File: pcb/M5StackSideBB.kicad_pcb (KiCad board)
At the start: 2 copper layers, 100 x 50 mm, 16 parts, among them J1 Conn_01x11, J2 Conn_01x11, J3 Conn_02x15_Odd_Even, J4 Conn_02x15_Odd_Even

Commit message: Change back logo size larger
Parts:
- removed G1: LOGO, logo:halake_25p5x18@5mm
- added G***: LOGO, logo:halake_44x32mm, B.Cu at (175.8, 77.4)

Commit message: Update design for production
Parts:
- removed G***: LOGO, logo:halake_44x32mm
- removed G2: LOGO, logo:halake_8p7px6p3mm
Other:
- board text added: "Rev 2018.08"
- board text added: "https://github.com/asukiaaa/M5StackSideBB"
- board text removed: "Rev 1.2"

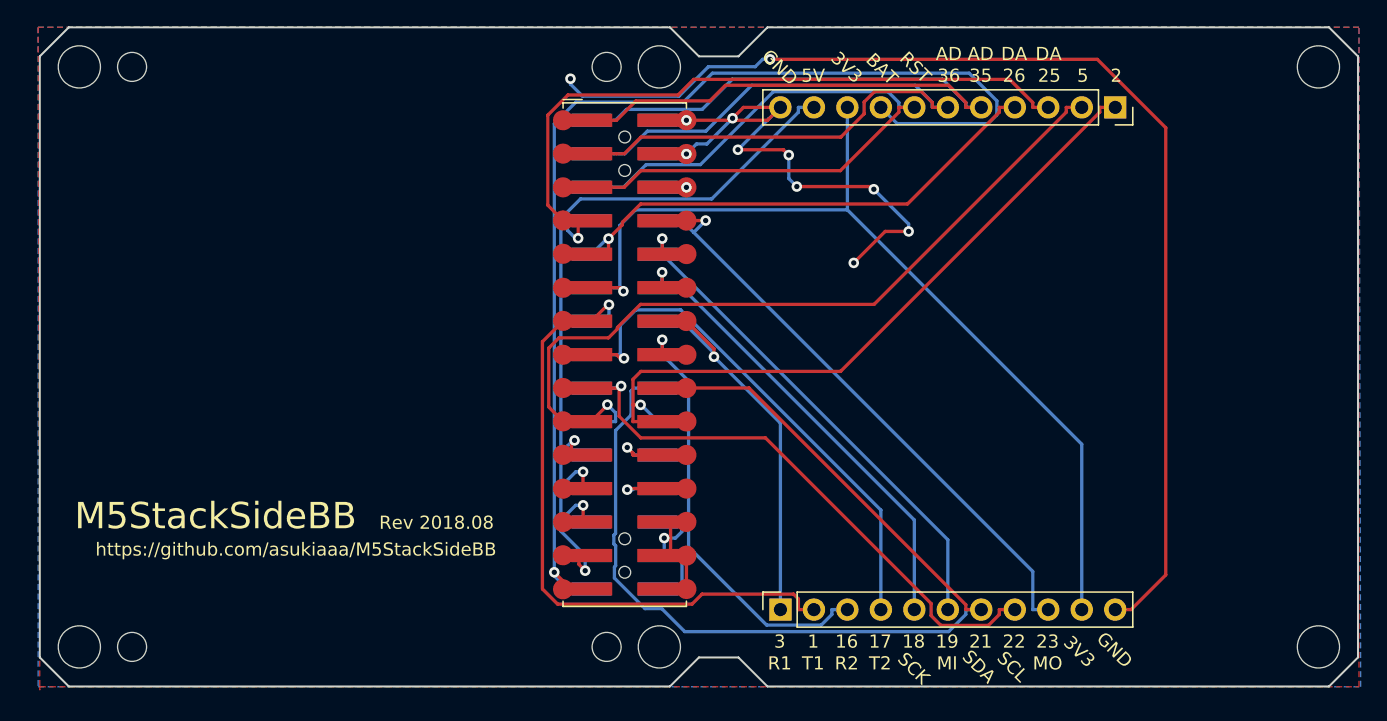
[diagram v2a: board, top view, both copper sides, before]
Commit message: Change pad position as Rev 2018.11
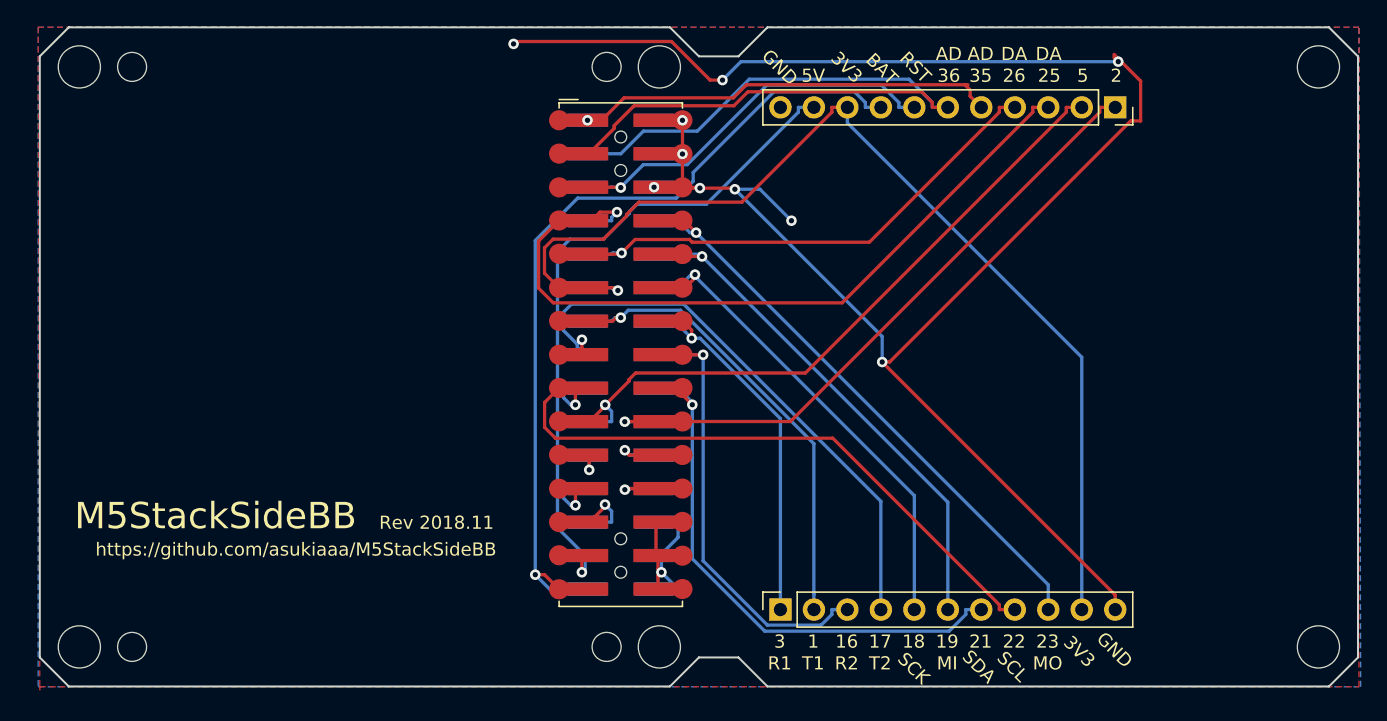
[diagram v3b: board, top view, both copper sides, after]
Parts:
- moved J3 0.30 mm to (144.1, 74.8)
- moved J4 0.30 mm to (144.1, 74.8)
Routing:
- net G21: track 79.1 -> 44.1 mm, vias 0 -> 1
- net G35: track 65.7 -> 34.4 mm, vias 0 -> 1
- net RST: track 57.6 -> 33.6 mm, vias 0 -> 1
- net +BATT: track 87.9 -> 66.5 mm
- net G1: track 49.7 -> 39.1 mm
- net +3V3: track 75.2 -> 83.6 mm
- net G5: track 61.6 -> 53.3 mm
- net GND: track 145.6 -> 153.5 mm, vias 12 -> 10
- net G22: track 46.8 -> 52.5 mm
- net G2: track 55.0 -> 49.5 mm
- net G17: track 43.6 -> 46.8 mm
- net G25: track 55.8 -> 58.6 mm
- net G13: track 6.60 -> 4.77 mm
- net G23: track 48.4 -> 46.8 mm
- net G18: track 38.0 -> 39.5 mm
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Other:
- board text added: "Rev 2018.11"
- board text removed: "Rev 2018.08"

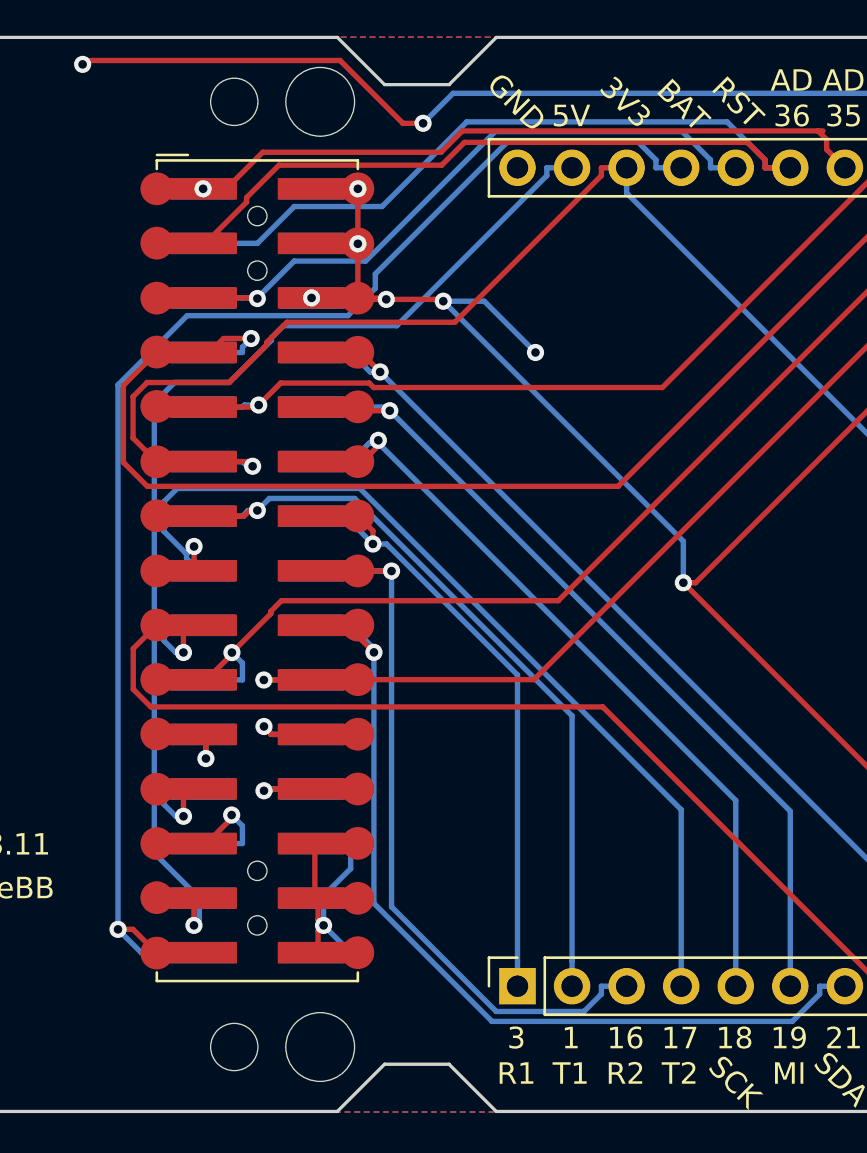
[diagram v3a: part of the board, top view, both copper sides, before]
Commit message: Add 4 holes to detect position of spacer_pcb
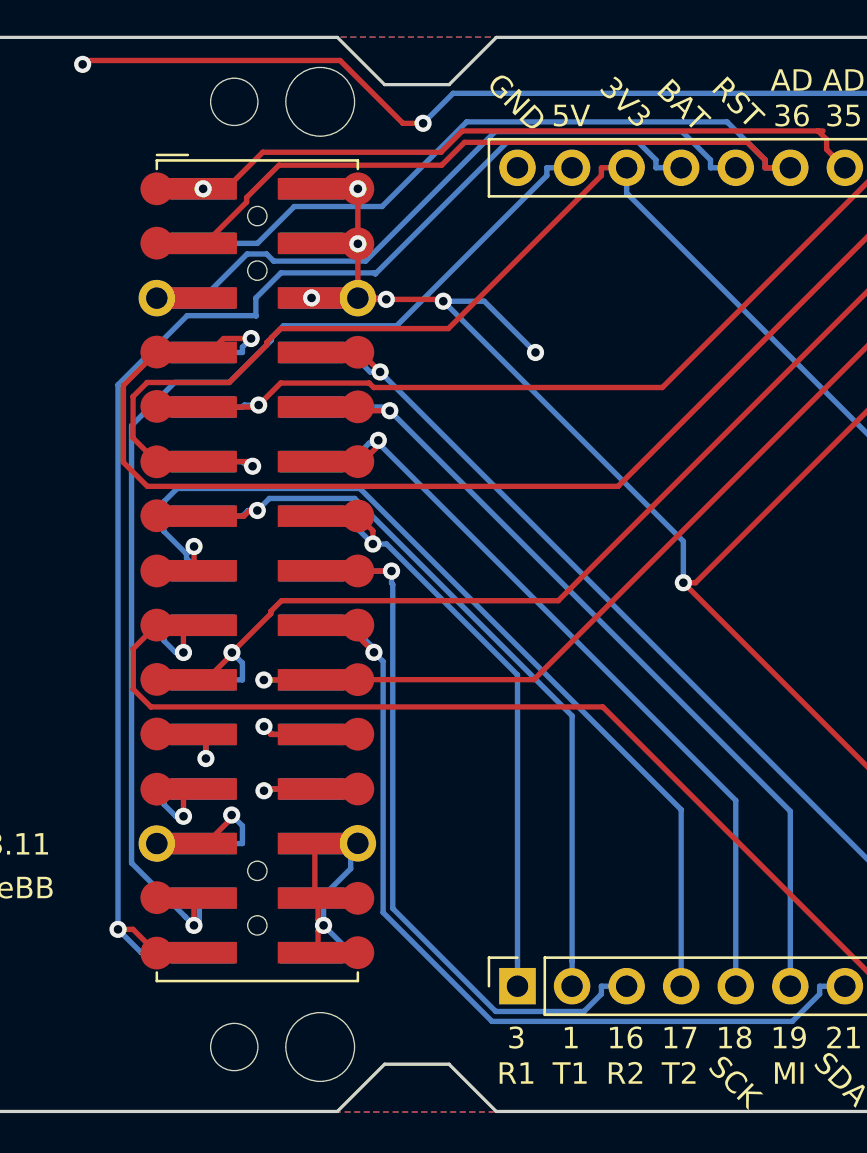
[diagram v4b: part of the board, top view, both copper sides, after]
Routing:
- net +5V: track 53.8 -> 55.8 mm
- net RST: track 33.6 -> 33.5 mm, vias 1 -> 0

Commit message: Add open source hardware logo
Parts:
- added REF**: OSHW-Logo2_7.3x6mm_SilkScreen, Symbol:OSHW-Logo2_7.3x6mm_SilkScreen, B.Cu at (188.2, 95.5)

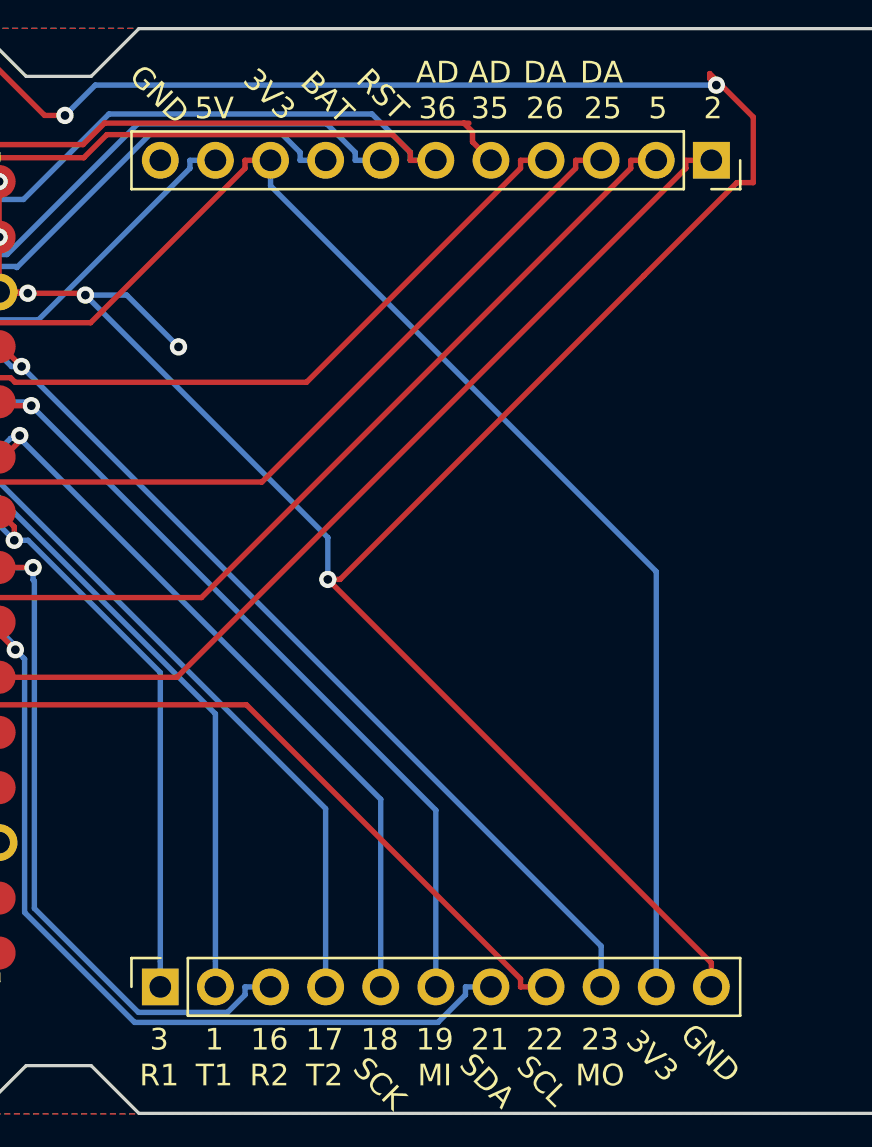
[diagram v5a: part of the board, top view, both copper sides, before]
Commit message: Assign footprint of pin socket without silk
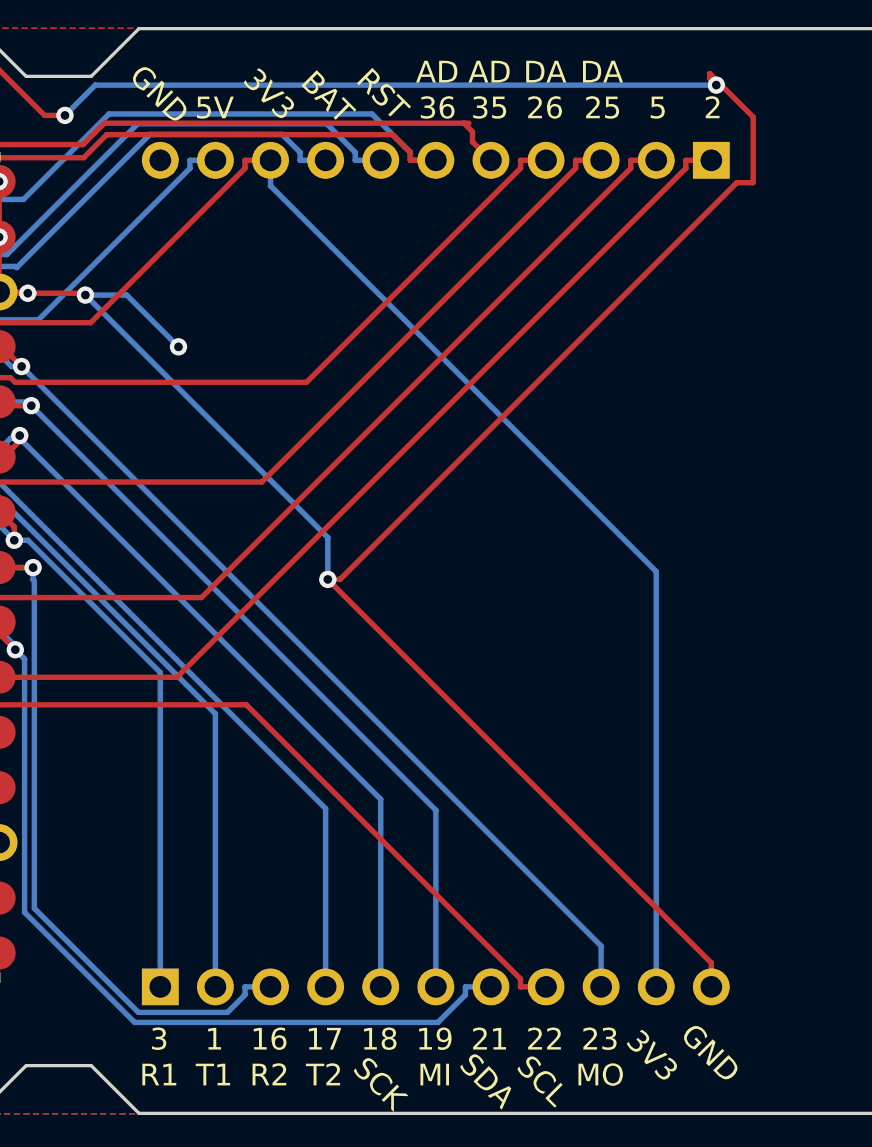
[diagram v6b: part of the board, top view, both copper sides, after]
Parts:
- J1, J2: footprint Connector_PinSocket_2.54mm:PinSocket_1x11_P2.54mm_Vertical -> footprints:PinSocket_1x11_P2.54mm_Vertical_without_silk

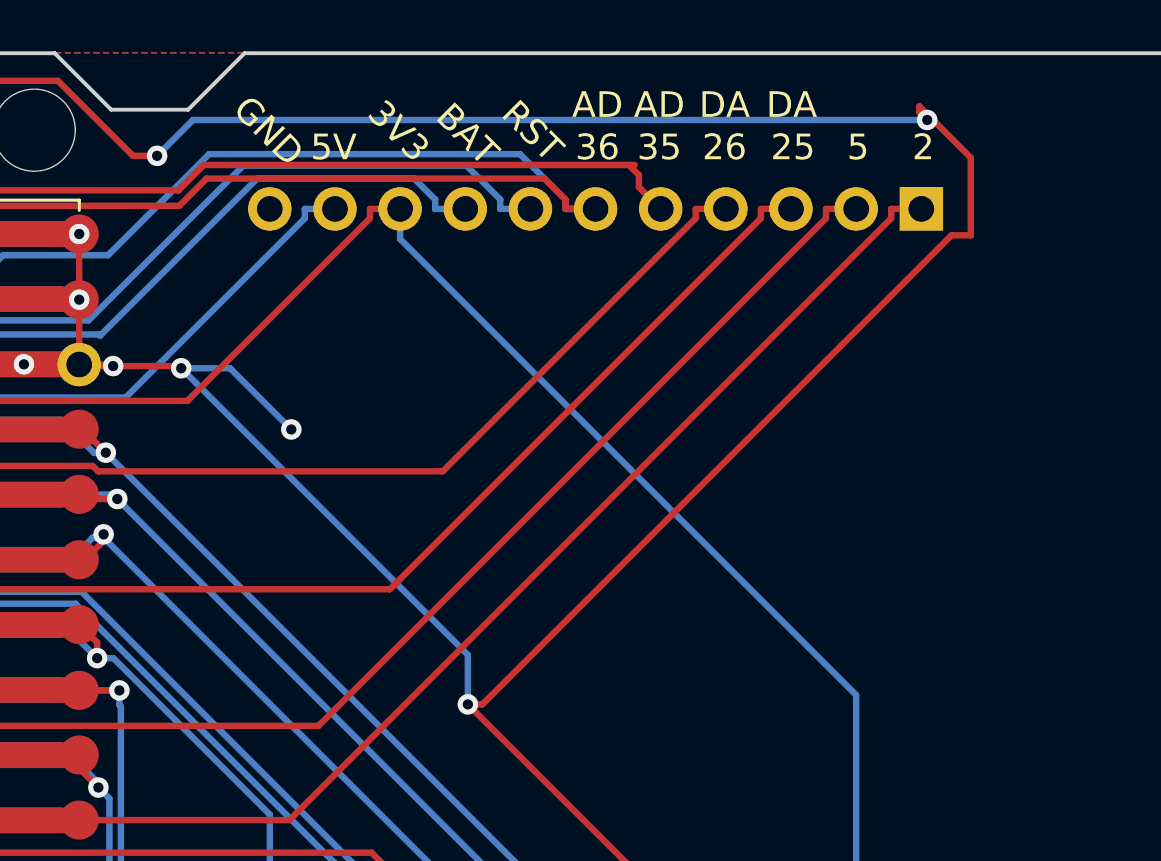
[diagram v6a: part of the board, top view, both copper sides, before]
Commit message: Change GND via position arround G2
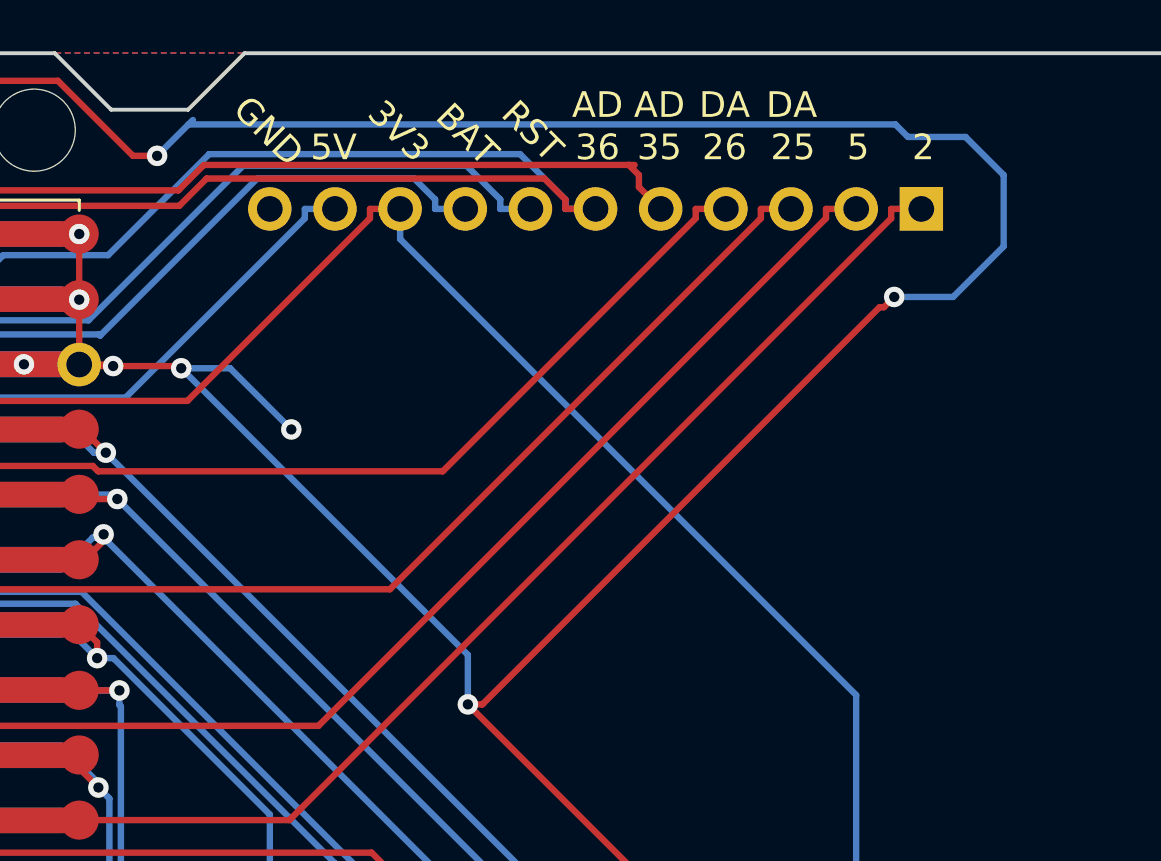
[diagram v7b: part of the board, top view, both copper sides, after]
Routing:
- net GND: track 153.5 -> 154.9 mm
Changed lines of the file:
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@@
     (thickness 1.6)
     (drawings 57)
-    (tracks 479)
+    (tracks 482)
     (zones 0)
     (modules 15)
@@
   (page A4)
   (layers
-    (0 F.Cu signal hide)
-    (31 B.Cu signal hide)
+    (0 F.Cu signal)
+    (31 B.Cu signal)
     (32 B.Adhes user)
     (33 F.Adhes user)
@@
   (segment (start 146.614 59.6084) (end 146.594 59.5884) (width 0.25) (layer B.Cu) (net 1))
   (segment (start 148.754 59.6084) (end 146.614 59.6084) (width 0.25) (layer B.Cu) (net 1))
-  (segment (start 164.471885 75.3872) (end 178.467285 61.3918) (width 0.25) (layer F.Cu) (net 1))
-  (segment (start 163.9062 75.3872) (end 164.471885 75.3872) (width 0.25) (layer F.Cu) (net 1))
-  (segment (start 182.760001 57.099084) (end 183.515116 57.099084) (width 0.25) (layer F.Cu) (net 1))
-  (segment (start 178.467285 61.3918) (end 182.760001 57.099084) (width 0.25) (layer F.Cu) (net 1))
-  (segment (start 183.515116 54.076716) (end 181.5084 52.07) (width 0.25) (layer F.Cu) (net 1))
-  (segment (start 183.515116 57.099084) (end 183.515116 54.076716) (width 0.25) (layer F.Cu) (net 1))
-  (segment (start 181.5084 52.07) (end 181.5084 52.2986) (width 0.25) (layer F.Cu) (net 1))
-  (via (at 181.8132 52.6034) (size 0.8) (drill 0.4) (layers F.Cu B.Cu) (net 1))
-  (segment (start 181.5084 52.2986) (end 181.8132 52.6034) (width 0.25) (layer F.Cu) (net 1))
   (via (at 151.7904 54.0004) (size 0.8) (drill 0.4) (layers F.Cu B.Cu) (net 1))
-  (segment (start 181.8132 52.6034) (end 153.1874 52.6034) (width 0.25) (layer B.Cu) (net 1))
-  (segment (start 153.1874 52.6034) (end 151.7904 54.0004) (width 0.25) (layer B.Cu) (net 1))
   (via (at 135.9408 51.2572) (size 0.8) (drill 0.4) (layers F.Cu B.Cu) (net 1))
   (segment (start 136.123001 51.074999) (end 135.9408 51.2572) (width 0.25) (layer F.Cu) (net 1))
@@
   (segment (start 151.7904 54.0004) (end 150.849402 54.0004) (width 0.25) (layer F.Cu) (net 1))
   (segment (start 150.849402 54.0004) (end 147.924001 51.074999) (width 0.25) (layer F.Cu) (net 1))
+  (segment (start 180.576122 52.77612) (end 181.063802 53.2638) (width 0.25) (layer B.Cu) (net 1))
+  (segment (start 153.01468 52.77612) (end 180.576122 52.77612) (width 0.25) (layer B.Cu) (net 1))
+  (segment (start 153.01468 52.77612) (end 151.7904 54.0004) (width 0.25) (layer B.Cu) (net 1))
+  (segment (start 153.1874 52.6034) (end 153.01468 52.77612) (width 0.25) (layer B.Cu) (net 1))
+  (segment (start 181.063802 53.2638) (end 183.30672 53.2638) (width 0.25) (layer B.Cu) (net 1))
+  (segment (start 183.30672 53.2638) (end 184.79516 54.75224) (width 0.25) (layer B.Cu) (net 1))
+  (segment (start 184.79516 54.75224) (end 184.79516 57.531) (width 0.25) (layer B.Cu) (net 1))
+  (via (at 180.52796 59.50204) (size 0.8) (drill 0.4) (layers F.Cu B.Cu) (net 1))
+  (segment (start 184.79516 57.531) (end 182.82412 59.50204) (width 0.25) (layer B.Cu) (net 1))
+  (segment (start 182.82412 59.50204) (end 180.52796 59.50204) (width 0.25) (layer B.Cu) (net 1))
+  (segment (start 164.471885 75.3872) (end 163.9062 75.3872) (width 0.25) (layer F.Cu) (net 1))
+  (segment (start 179.957046 59.902039) (end 164.471885 75.3872) (width 0.25) (layer F.Cu) (net 1))
+  (segment (start 180.127961 59.902039) (end 179.957046 59.902039) (width 0.25) (layer F.Cu) (net 1))
+  (segment (start 180.52796 59.50204) (end 180.127961 59.902039) (width 0.25) (layer F.Cu) (net 1))
   (segment (start 149.7905 65.5745) (end 176.505 92.289) (width 0.25) (layer B.Cu) (net 2))
   (segment (start 176.505 92.289) (end 176.505 94.17) (width 0.25) (layer B.Cu) (net 2))

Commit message: Update revision as 2018.12
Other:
- board text added: "Rev 2018.12"
- board text removed: "Rev 2018.11"
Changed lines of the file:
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@@
     )
   )
-  (gr_text "Rev 2018.11" (at 130.0988 87.5792) (layer F.SilkS)
+  (gr_text "Rev 2018.12" (at 130.0988 87.5792) (layer F.SilkS)
     (effects (font (size 1 1) (thickness 0.25)))
   )
@@
     (effects (font (size 1 1) (thickness 0.25)))
   )
-  (gr_text "Rev 2018.11" (at 160.43148 87.88908) (layer B.SilkS)
+  (gr_text "Rev 2018.12" (at 160.43148 87.88908) (layer B.SilkS)
     (effects (font (size 1.2 1.2) (thickness 0.3)) (justify mirror))
   )
